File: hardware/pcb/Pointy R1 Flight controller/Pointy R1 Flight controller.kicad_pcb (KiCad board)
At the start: 2 copper layers, 60 x 100 mm, 30 parts, among them IC1 TEENSY_4.1, J3 XT60-M, M1 Motor_Servo, M2 Motor_Servo, P1 282837-2, P2 282837-2, P3 282837-2, P4 282837-2, Q1 IRLZ44NSTRLPBF, Q2 IRLZ44NSTRLPBF, Q3 IRLZ44NSTRLPBF, U1 L7805CV, U2 GY-521, U3 MPL3115A2

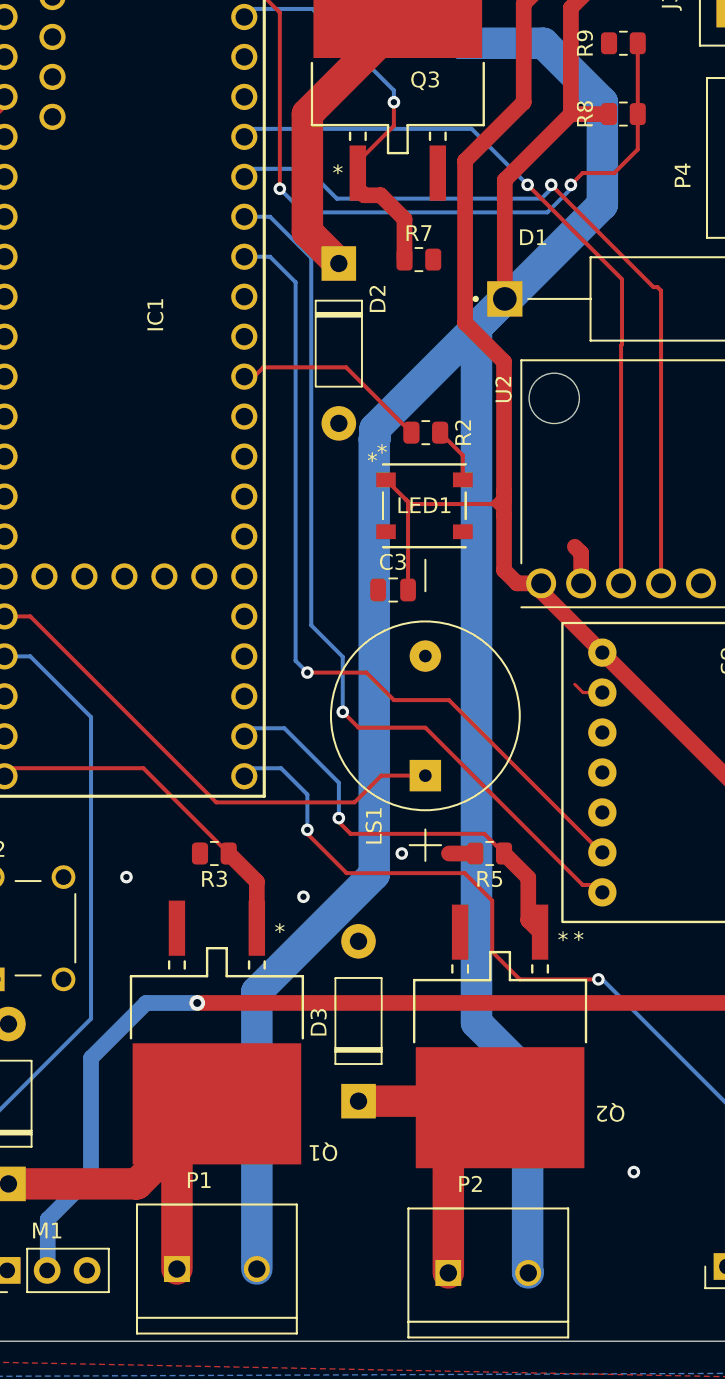
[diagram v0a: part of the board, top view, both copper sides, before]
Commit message: Updated PCB files to conform with DFM and regenerated gerbers. PCB ready for manufacture
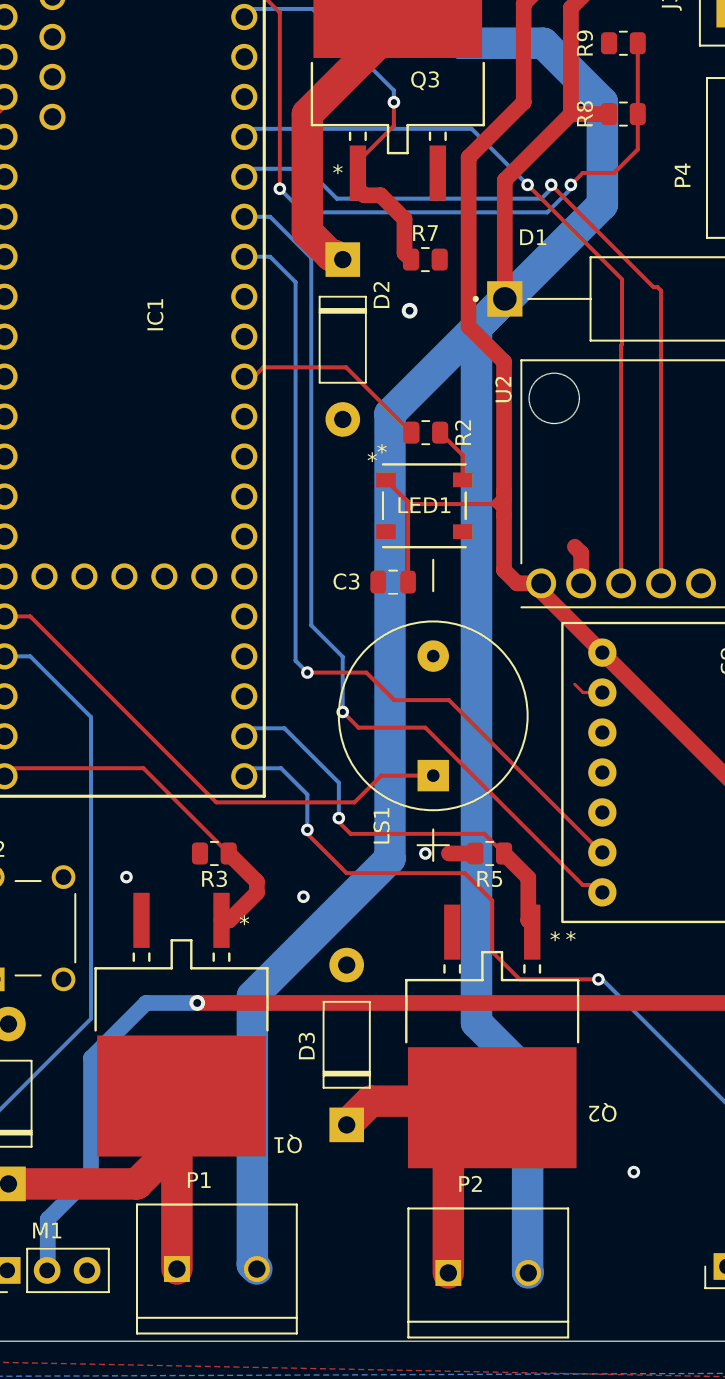
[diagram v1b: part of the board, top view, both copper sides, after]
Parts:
- moved Q1 2.30 mm to (130.5, 142.0)
- moved D3 1.68 mm to (141.0, 147.0)
- moved C3 0.50 mm to (143.9, 112.5)
- moved LS1 0.50 mm to (146.5, 121.0)
- moved Q2 0.50 mm to (150.2, 142.8)
- moved R7 0.41 mm to (146.0, 92.0)
- moved D2 0.35 mm to (140.8, 92.0)
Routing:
- net Net-(D4-A): track 26.9 -> 24.4 mm
- net Net-(D3-A): track 20.7 -> 21.6 mm
- net PY1: track 22.2 -> 22.9 mm
- net +5V: track 205.9 -> 205.2 mm
- net BUZ: track 32.4 -> 32.9 mm
- net GND: vias 5 -> 6

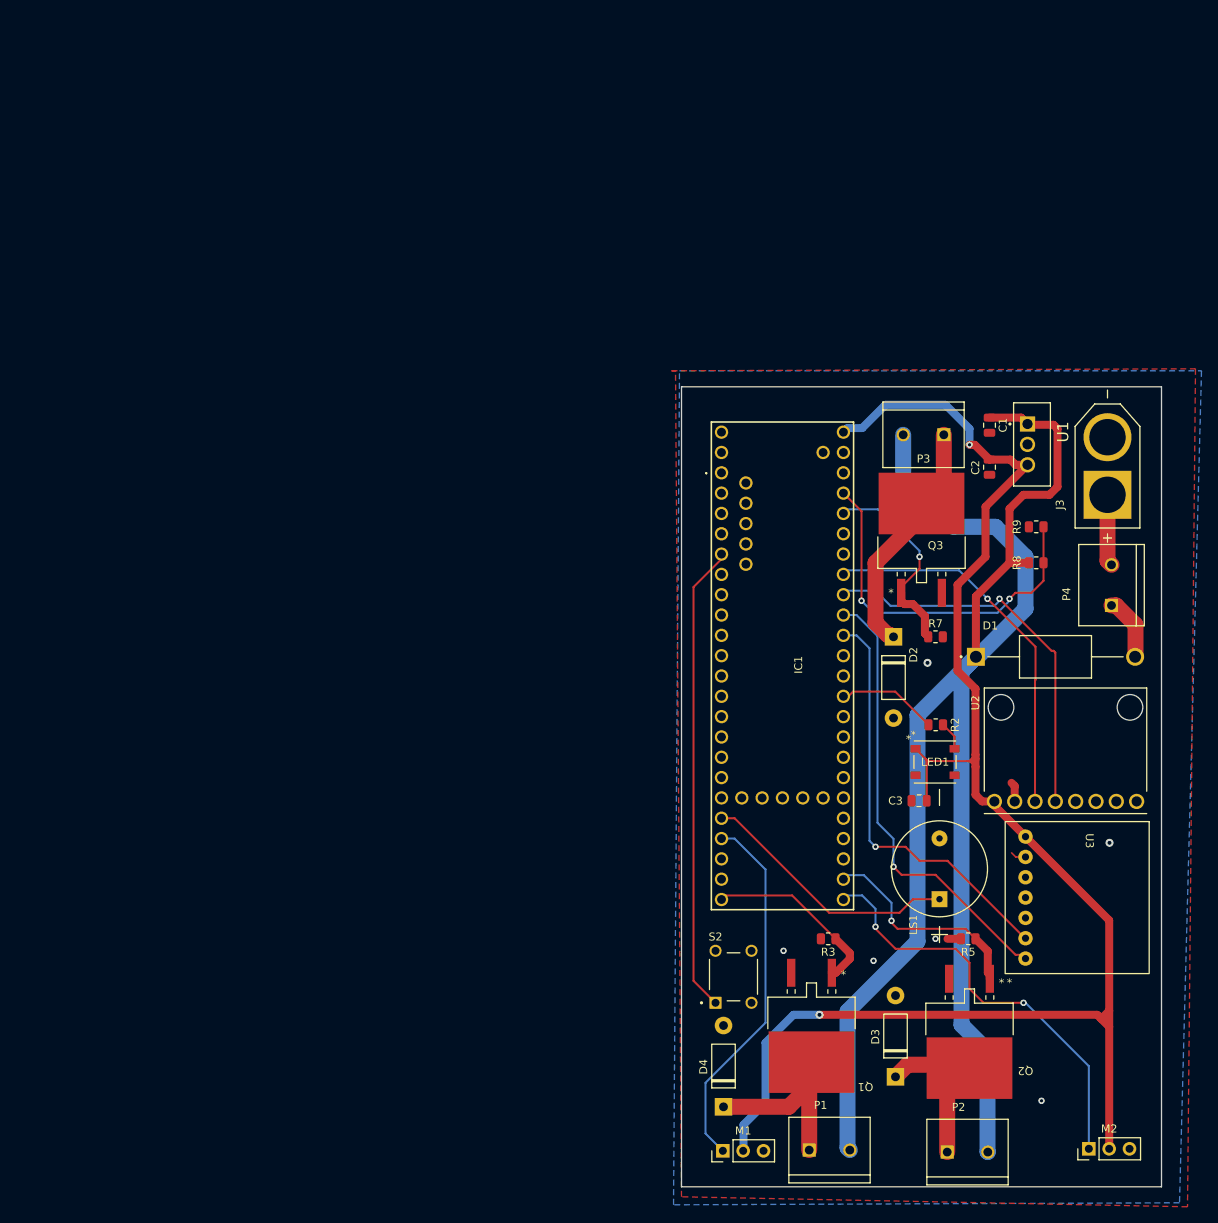
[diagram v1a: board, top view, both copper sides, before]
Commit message: Added 3d Models to PCB for teensy + Mosfets
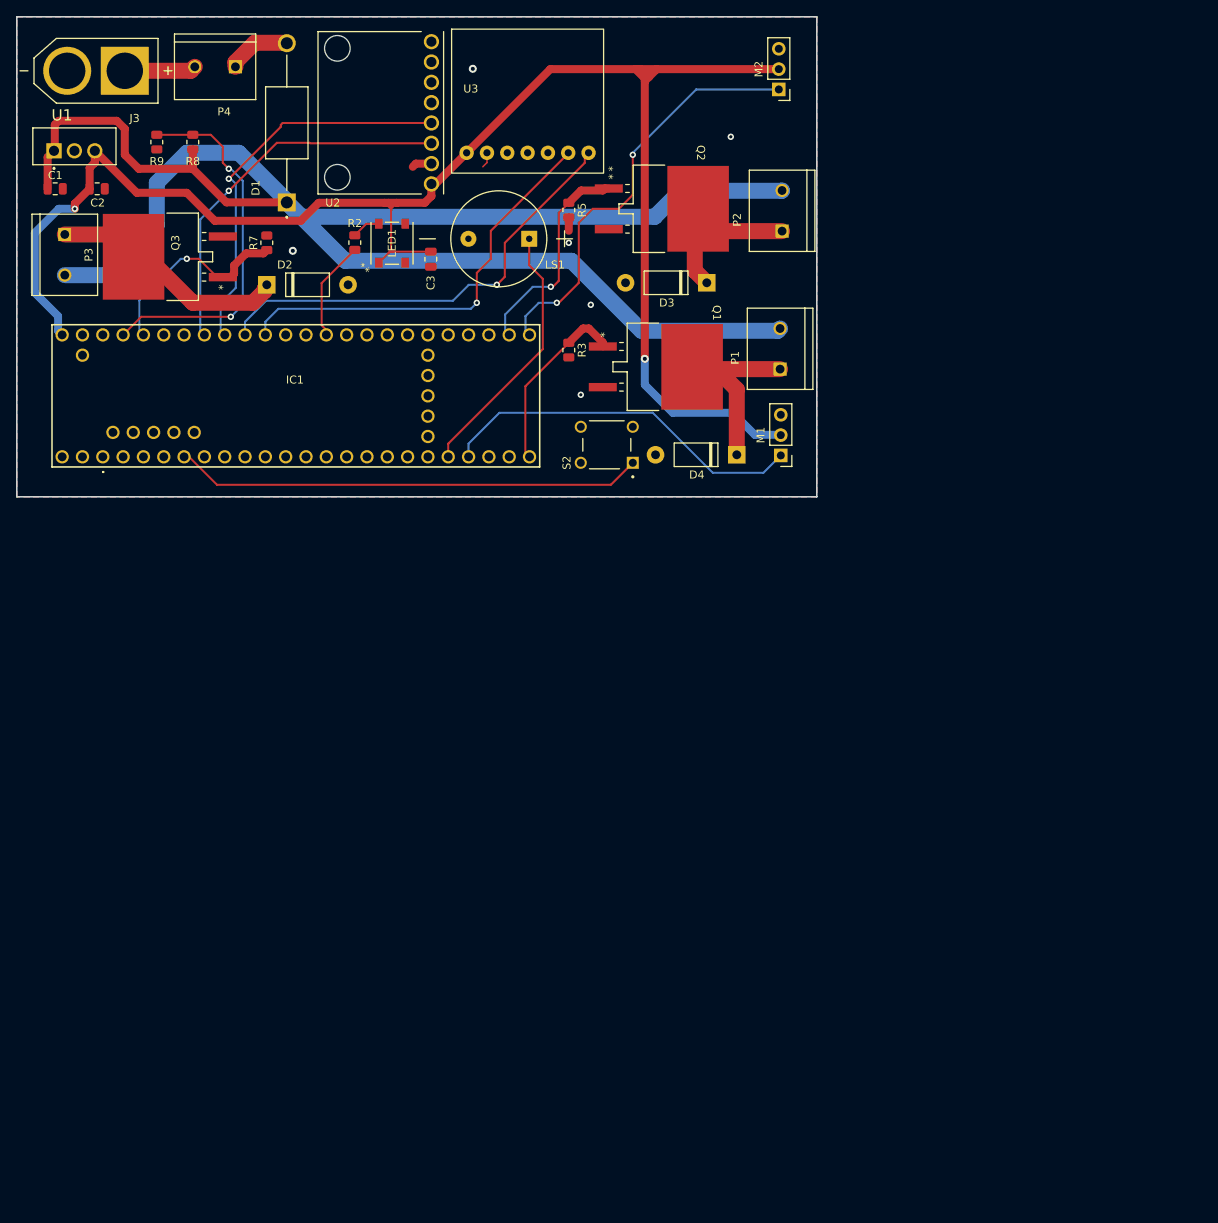
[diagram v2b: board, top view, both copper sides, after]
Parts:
- moved M2 138.0 mm to (126.4, 23.6), turned to 180 degrees
- moved J3 135.7 mm to (41.1, 21.2), turned to 180 degrees
- moved P4 129.4 mm to (56.0, 20.8), turned to 180 degrees
- moved U1 126.4 mm to (35.8, 31.2), turned to 0 degrees
- moved C1 120.5 mm to (36.0, 36.0), turned to 0 degrees
- moved R9 120.0 mm to (48.7, 30.2), turned to 90 degrees
- moved P2 119.9 mm to (126.8, 38.8), turned to 90 degrees
- moved R8 117.8 mm to (53.2, 30.2), turned to 90 degrees
- moved D1 117.0 mm to (64.9, 27.8), turned to 90 degrees
- moved U2 117.0 mm to (76.7, 26.5), turned to 180 degrees
- moved C2 116.8 mm to (41.2, 36.0), turned to 0 degrees
- moved Q2 110.7 mm to (113.2, 38.5), turned to -90 degrees
- moved P3 109.7 mm to (37.2, 44.2), turned to -90 degrees
- moved U3 108.5 mm to (95.0, 34.0), turned to 0 degrees
- moved R5 103.9 mm to (100.2, 38.7), turned to -90 degrees
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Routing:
- net +5V: track 205.2 -> 207.2 mm
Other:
- board size 60 x 100 mm -> 100 x 60 mm
